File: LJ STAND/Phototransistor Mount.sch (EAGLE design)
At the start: 3 parts

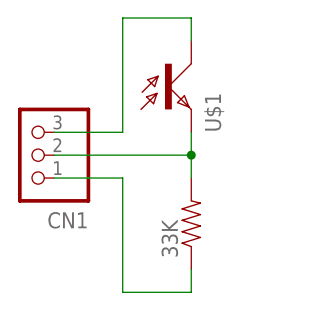
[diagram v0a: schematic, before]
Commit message: Finalisation of gyro, encoder and light boards + gerbers, silkscreen fixes
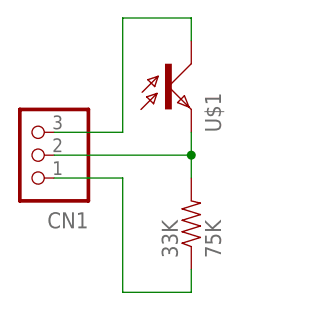
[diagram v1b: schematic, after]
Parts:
- 33K: value (none) -> 75K
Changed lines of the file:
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@@
 <part name="U$1" library="phototransitor-ALS-PT19-315CL177TR8" library_urn="urn:adsk.eagle:library:1968580" deviceset="ALS" device="" package3d_urn="urn:adsk.eagle:package:1968583/2"/>
 <part name="CN1" library="jst-ph" library_urn="urn:adsk.eagle:library:1951258" deviceset="B3B-PH-*" device="K-S" package3d_urn="urn:adsk.eagle:package:1951338/1"/>
-<part name="33K" library="SparkFun-Passives" deviceset="RESISTOR" device="0603-RES"/>
+<part name="33K" library="SparkFun-Passives" deviceset="RESISTOR" device="0603-RES" value="75K"/>
 </parts>
 <sheets>

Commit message: Pin changes on teensys, removed some screen pins for motor grounding
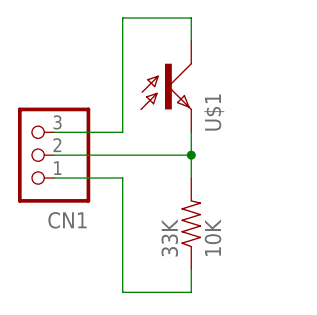
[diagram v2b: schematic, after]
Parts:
- 33K: value 75K -> 10K
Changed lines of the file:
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@@
 <part name="U$1" library="phototransitor-ALS-PT19-315CL177TR8" library_urn="urn:adsk.eagle:library:1968580" deviceset="ALS" device="" package3d_urn="urn:adsk.eagle:package:1968583/2"/>
 <part name="CN1" library="jst-ph" library_urn="urn:adsk.eagle:library:1951258" deviceset="B3B-PH-*" device="K-S" package3d_urn="urn:adsk.eagle:package:1951338/1"/>
-<part name="33K" library="SparkFun-Passives" deviceset="RESISTOR" device="0603-RES" value="75K"/>
+<part name="33K" library="SparkFun-Passives" deviceset="RESISTOR" device="0603-RES" value="10K"/>
 </parts>
 <sheets>

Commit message: Gyro MPU9250 boards
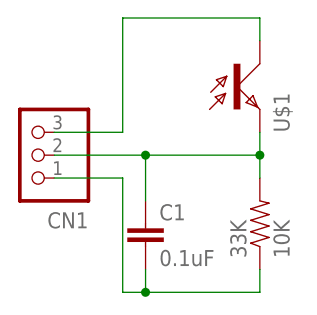
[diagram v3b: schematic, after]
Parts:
- added C1: 0.1uF, SparkFun-Capacitors:CAP0603-CAP
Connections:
- net N$2: now also C1.2
- net OUT: now also C1.1
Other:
- moved on the sheet: 33K, U$1
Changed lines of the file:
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@@
 <part name="CN1" library="jst-ph" library_urn="urn:adsk.eagle:library:1951258" deviceset="B3B-PH-*" device="K-S" package3d_urn="urn:adsk.eagle:package:1951338/1"/>
 <part name="33K" library="SparkFun-Passives" deviceset="RESISTOR" device="0603-RES" value="10K"/>
+<part name="C1" library="SparkFun-Capacitors" deviceset="CAP" device="0603-CAP" value="0.1uF"/>
 </parts>
 <sheets>
@@
 </plain>
 <instances>
-<instance part="U$1" gate="G$1" x="53.34" y="63.5"/>
+<instance part="U$1" gate="G$1" x="60.96" y="63.5"/>
 <instance part="CN1" gate="G$1" x="40.64" y="55.88" rot="R180"/>
-<instance part="33K" gate="G$1" x="55.88" y="48.26" rot="R90"/>
+<instance part="33K" gate="G$1" x="63.5" y="48.26" rot="R90"/>
+<instance part="C1" gate="G$1" x="50.8" y="45.72"/>
 </instances>
 <busses>
@@
 <pinref part="U$1" gate="G$1" pin="E"/>
 <pinref part="33K" gate="G$1" pin="2"/>
-<wire x1="55.88" y1="53.34" x2="55.88" y2="55.88" width="0.1524" layer="91"/>
+<wire x1="63.5" y1="53.34" x2="63.5" y2="55.88" width="0.1524" layer="91"/>
 <pinref part="CN1" gate="G$1" pin="2"/>
-<wire x1="55.88" y1="55.88" x2="55.88" y2="58.42" width="0.1524" layer="91"/>
-<wire x1="55.88" y1="55.88" x2="40.64" y2="55.88" width="0.1524" layer="91"/>
-<junction x="55.88" y="55.88"/>
+<wire x1="63.5" y1="55.88" x2="63.5" y2="58.42" width="0.1524" layer="91"/>
+<wire x1="63.5" y1="55.88" x2="50.8" y2="55.88" width="0.1524" layer="91"/>
+<junction x="63.5" y="55.88"/>
+<pinref part="C1" gate="G$1" pin="1"/>
+<wire x1="50.8" y1="55.88" x2="40.64" y2="55.88" width="0.1524" layer="91"/>
+<wire x1="50.8" y1="50.8" x2="50.8" y2="55.88" width="0.1524" layer="91"/>
+<junction x="50.8" y="55.88"/>
 </segment>
 </net>
@@
 <segment>
 <pinref part="U$1" gate="G$1" pin="C"/>
-<wire x1="55.88" y1="68.58" x2="55.88" y2="71.12" width="0.1524" layer="91"/>
-<wire x1="55.88" y1="71.12" x2="48.26" y2="71.12" width="0.1524" layer="91"/>
+<wire x1="63.5" y1="68.58" x2="63.5" y2="71.12" width="0.1524" layer="91"/>
+<wire x1="63.5" y1="71.12" x2="48.26" y2="71.12" width="0.1524" layer="91"/>
 <wire x1="48.26" y1="71.12" x2="48.26" y2="58.42" width="0.1524" layer="91"/>
 <pinref part="CN1" gate="G$1" pin="3"/>
@@
 <segment>
 <pinref part="33K" gate="G$1" pin="1"/>
-<wire x1="55.88" y1="40.64" x2="55.88" y2="43.18" width="0.1524" layer="91"/>
+<wire x1="63.5" y1="40.64" x2="63.5" y2="43.18" width="0.1524" layer="91"/>
 <pinref part="CN1" gate="G$1" pin="1"/>
 <wire x1="40.64" y1="53.34" x2="48.26" y2="53.34" width="0.1524" layer="91"/>
 <wire x1="48.26" y1="53.34" x2="48.26" y2="40.64" width="0.1524" layer="91"/>
-<wire x1="48.26" y1="40.64" x2="55.88" y2="40.64" width="0.1524" layer="91"/>
+<wire x1="48.26" y1="40.64" x2="50.8" y2="40.64" width="0.1524" layer="91"/>
+<pinref part="C1" gate="G$1" pin="2"/>
+<wire x1="50.8" y1="40.64" x2="63.5" y2="40.64" width="0.1524" layer="91"/>
+<wire x1="50.8" y1="43.18" x2="50.8" y2="40.64" width="0.1524" layer="91"/>
+<junction x="50.8" y="40.64"/>
 </segment>
 </net>
